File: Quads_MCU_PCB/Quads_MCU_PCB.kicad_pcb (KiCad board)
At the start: 4 copper layers, 100 x 100 mm, 108 parts, among them J1 USB_C_Receptacle_USB2.0_16P, J2 Conn_01x06_Pin, J3 Conn_01x02_Pin, J4 Conn_01x04_Pin, J5 Conn_01x04_Pin, J6 Conn_01x04_Pin, J7 Conn_01x04_Pin, SW1 SW_Push, U1 STM32H723ZGTx, U10 BMI088, U3 ADM3057ExRW, U4 TSR_1-2450, U5 AP7361C-33E, U6 ADM3057ExRW, U7 ADM3057ExRW, U8 MCP2518FD-xQBB, U9 ADM3057ExRW, Y1 40MHz, Y2 25MHz

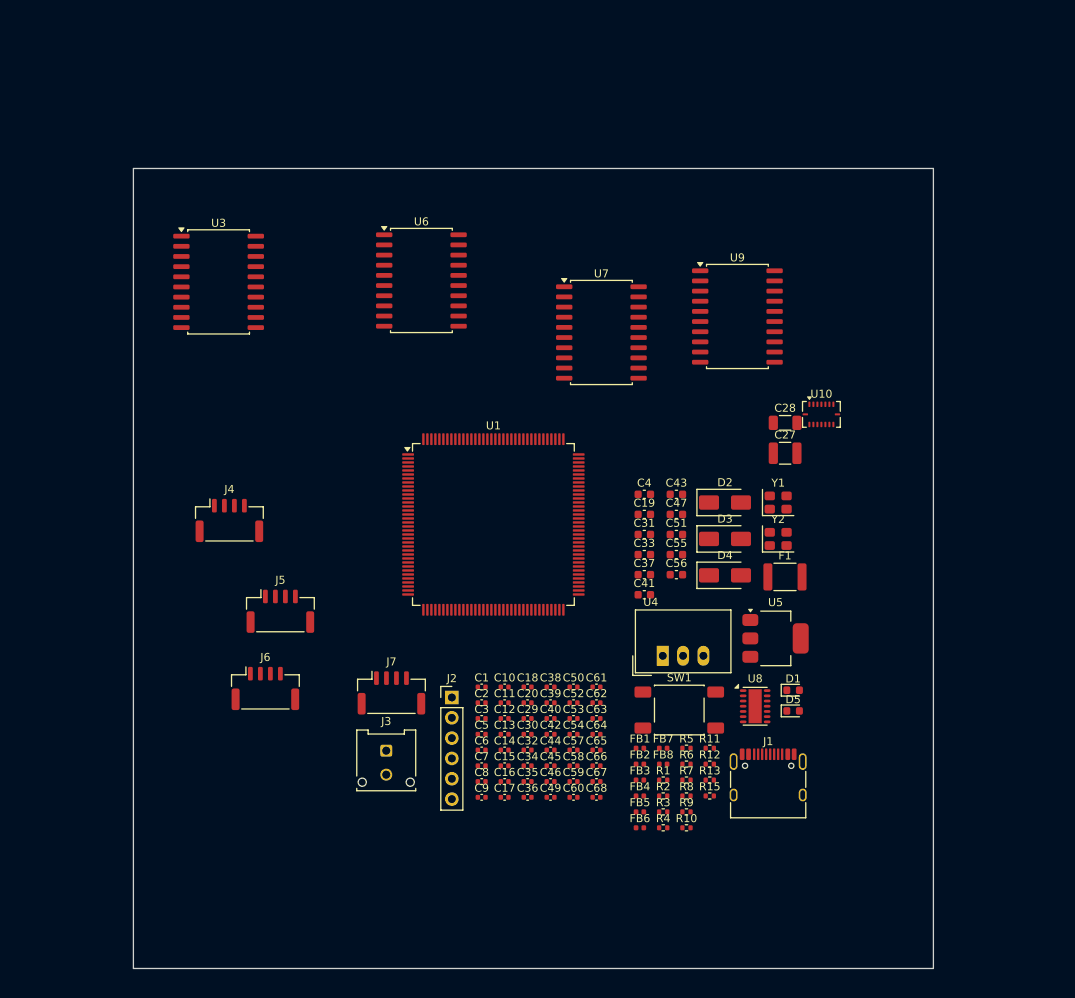
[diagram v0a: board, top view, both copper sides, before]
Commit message: Updated pwr connector footprint & added 3d model
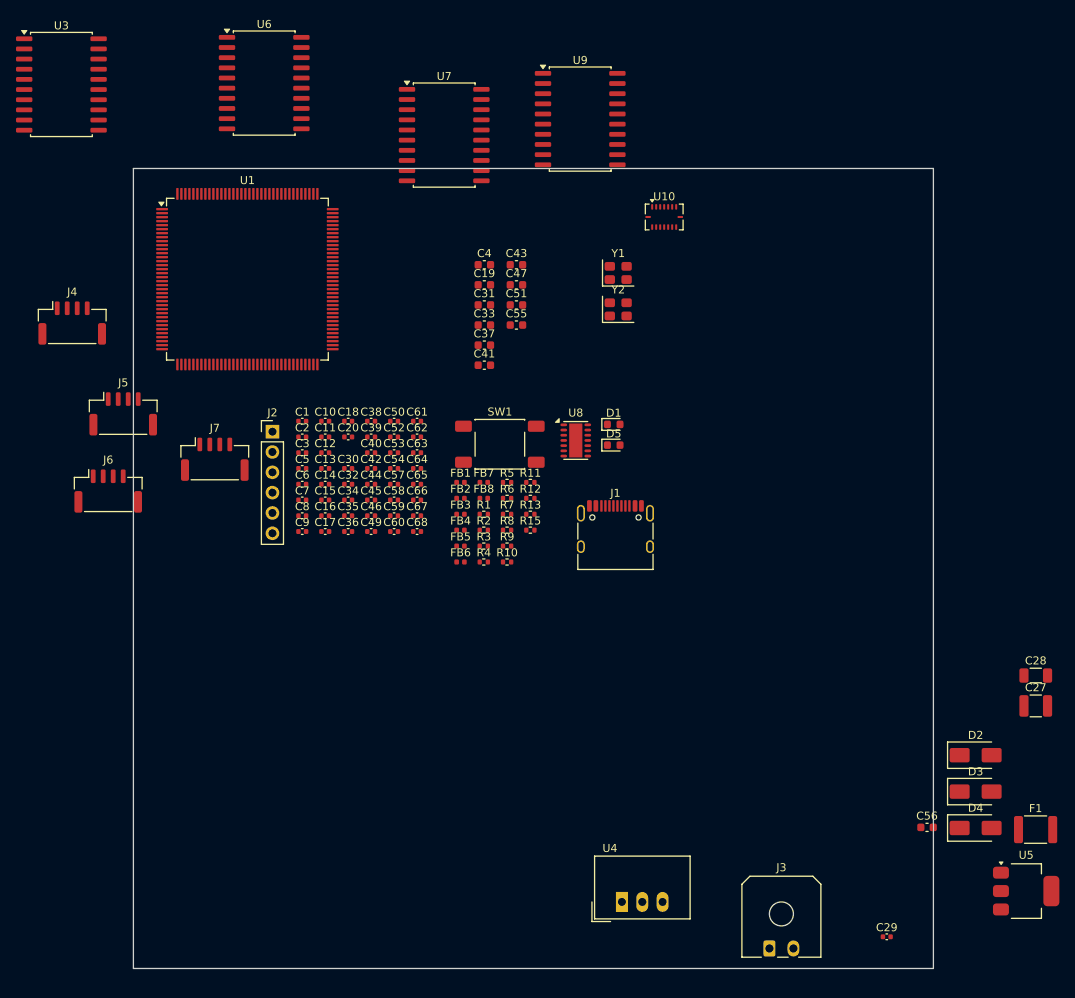
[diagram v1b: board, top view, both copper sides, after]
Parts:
- J3: footprint Connector_Molex:Molex_Micro-Fit_3.0_43045-0212_2x01_P3.00mm_Vertical -> Connector_Molex:Molex_Micro-Fit_3.0_43650-0200_1x02_P3.00mm_Horizontal
- moved J3 53.9 mm to (113.5, 136.0)
- moved C29 52.5 mm to (128.2, 134.5)
- moved C56 44.5 mm to (133.2, 120.9)
- moved F1 44.5 mm to (146.8, 121.1)
- moved D2 44.5 mm to (139.3, 111.8)
- moved D3 44.5 mm to (139.3, 116.4)
- moved D4 44.5 mm to (139.3, 120.9)
- moved U5 44.5 mm to (145.6, 128.8)
- moved C27 44.5 mm to (146.8, 105.7)
- moved C28 44.5 mm to (146.8, 101.9)
- moved U1 43.4 mm to (48.2, 52.3)
- moved C66 40.1 mm to (69.5, 79.9)
- moved C67 40.1 mm to (69.5, 81.9)
- moved C68 40.1 mm to (69.5, 83.9)
- moved R10 40.1 mm to (80.7, 87.7)
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
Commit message: Updated molex connector position
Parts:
- moved J3 8.06 mm to (117.5, 129.0), turned to 180 degrees
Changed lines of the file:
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@@
 	(footprint "Connector_Molex:Molex_Micro-Fit_3.0_43650-0200_1x02_P3.00mm_Horizontal"
 		(layer "F.Cu")
-		(at 113.5 136)
+		(at 117.5 129 180)
 		(descr "Molex Micro-Fit 3.0 Connector System, 43650-0200 (compatible alternatives: 43650-0201, 43650-0202), 2 Pins per row (https://www.molex.com/pdm_docs/sd/436500300_sd.pdf)")
 		(tags "connector Molex Micro-Fit_3.0 horizontal")
@@
 		)
 		(property "LCSC" "C293362"
-			(at 0 0 0)
+			(at 0 0 180)
 			(unlocked yes)
 			(layer "F.Fab")
@@
 		(duplicate_pad_numbers_are_jumpers no)
 		(fp_line
+			(start 6.435 1.09)
+			(end 3.651767 1.09)
+			(stroke
+				(width 0.12)
+				(type solid)
+			)
+			(layer "F.SilkS")
+		)
+		(fp_line
+			(start 6.435 -8.03)
+			(end 6.435 1.09)
+			(stroke
+				(width 0.12)
+				(type solid)
+			)
+			(layer "F.SilkS")
+		)
+		(fp_line
+			(start 5.435 -9.03)
+			(end 6.435 -8.03)
+			(stroke
+				(width 0.12)
+				(type solid)
+			)
+			(layer "F.SilkS")
+		)
+		(fp_line
+			(start 1.01 1.09)
+			(end 2.348233 1.09)
+			(stroke
+				(width 0.12)
+				(type solid)
+			)
+			(layer "F.SilkS")
+		)
+		(fp_line
+			(start -2.435 -9.03)
+			(end 5.435 -9.03)
+			(stroke
+				(width 0.12)
+				(type solid)
+			)
+			(layer "F.SilkS")
+		)
+		(fp_line
+			(start -3.435 1.09)
+			(end -1.01 1.09)
+			(stroke
+				(width 0.12)
+				(type solid)
+			)
+			(layer "F.SilkS")
+		)
+		(fp_line
+			(start -3.435 1.09)
+			(end -3.435 -8.03)
+			(stroke
+				(width 0.12)
+				(type solid)
+			)
+			(layer "F.SilkS")
+		)
+		(fp_line
 			(start -3.435 -8.03)
 			(end -2.435 -9.03)
@@
 		)
 		(fp_line
-			(start -3.435 1.09)
-			(end -3.435 -8.03)
-			(stroke
-				(width 0.12)
-				(type solid)
-			)
-			(layer "F.SilkS")
-		)
-		(fp_line
-			(start -3.435 1.09)
-			(end -1.01 1.09)
-			(stroke
-				(width 0.12)
-				(type solid)
-			)
-			(layer "F.SilkS")
-		)
-		(fp_line
-			(start -2.435 -9.03)
-			(end 5.435 -9.03)
-			(stroke
-				(width 0.12)
-				(type solid)
-			)
-			(layer "F.SilkS")
-		)
-		(fp_line
-			(start 1.01 1.09)
-			(end 2.348233 1.09)
-			(stroke
-				(width 0.12)
-				(type solid)
-			)
-			(layer "F.SilkS")
-		)
-		(fp_line
-			(start 5.435 -9.03)
-			(end 6.435 -8.03)
-			(stroke
-				(width 0.12)
-				(type solid)
-			)
-			(layer "F.SilkS")
-		)
-		(fp_line
-			(start 6.435 -8.03)
-			(end 6.435 1.09)
-			(stroke
-				(width 0.12)
-				(type solid)
-			)
-			(layer "F.SilkS")
-		)
-		(fp_line
-			(start 6.435 1.09)
-			(end 3.651767 1.09)
-			(stroke
-				(width 0.12)
-				(type solid)
-			)
-			(layer "F.SilkS")
+			(start 6.83 1.49)
+			(end -3.83 1.49)
+			(stroke
+				(width 0.05)
+				(type solid)
+			)
+			(layer "F.CrtYd")
+		)
+		(fp_line
+			(start 6.83 -9.42)
+			(end 6.83 1.49)
+			(stroke
+				(width 0.05)
+				(type solid)
+			)
+			(layer "F.CrtYd")
+		)
+		(fp_line
+			(start -3.83 1.49)
+			(end -3.83 -9.42)
+			(stroke
+				(width 0.05)
+				(type solid)
+			)
+			(layer "F.CrtYd")
 		)
 		(fp_line
@@
 		)
 		(fp_line
-			(start -3.83 1.49)
-			(end -3.83 -9.42)
-			(stroke
-				(width 0.05)
-				(type solid)
-			)
-			(layer "F.CrtYd")
-		)
-		(fp_line
-			(start 6.83 -9.42)
-			(end 6.83 1.49)
-			(stroke
-				(width 0.05)
-				(type solid)
-			)
-			(layer "F.CrtYd")
-		)
-		(fp_line
-			(start 6.83 1.49)
-			(end -3.83 1.49)
-			(stroke
-				(width 0.05)
-				(type solid)
-			)
-			(layer "F.CrtYd")
+			(start 6.325 0.98)
+			(end -3.325 0.98)
+			(stroke
+				(width 0.1)
+				(type solid)
+			)
+			(layer "F.Fab")
+		)
+		(fp_line
+			(start 6.325 -7.92)
+			(end 6.325 0.98)
+			(stroke
+				(width 0.1)
+				(type solid)
+			)
+			(layer "F.Fab")
+		)
+		(fp_line
+			(start 5.325 -8.92)
+			(end 6.325 -7.92)
+			(stroke
+				(width 0.1)
+				(type solid)
+			)
+			(layer "F.Fab")
+		)
+		(fp_line
+			(start 0 0)
+			(end 0.75 0.98)
+			(stroke
+				(width 0.1)
+				(type solid)
+			)
+			(layer "F.Fab")
+		)
+		(fp_line
+			(start -0.75 0.98)
+			(end 0 0)
+			(stroke
+				(width 0.1)
+				(type solid)
+			)
+			(layer "F.Fab")
+		)
+		(fp_line
+			(start -2.325 -8.92)
+			(end 5.325 -8.92)
+			(stroke
+				(width 0.1)
+				(type solid)
+			)
+			(layer "F.Fab")
+		)
+		(fp_line
+			(start -3.325 0.98)
+			(end -3.325 -7.92)
+			(stroke
+				(width 0.1)
+				(type solid)
+			)
+			(layer "F.Fab")
 		)
 		(fp_line
@@
 			(layer "F.Fab")
 		)
-		(fp_line
-			(start -3.325 0.98)
-			(end -3.325 -7.92)
-			(stroke
-				(width 0.1)
-				(type solid)
-			)
-			(layer "F.Fab")
-		)
-		(fp_line
-			(start -2.325 -8.92)
-			(end 5.325 -8.92)
-			(stroke
-				(width 0.1)
-				(type solid)
-			)
-			(layer "F.Fab")
-		)
-		(fp_line
-			(start -0.75 0.98)
-			(end 0 0)
-			(stroke
-				(width 0.1)
-				(type solid)
-			)
-			(layer "F.Fab")
-		)
-		(fp_line
-			(start 0 0)
-			(end 0.75 0.98)
-			(stroke
-				(width 0.1)
-				(type solid)
-			)
-			(layer "F.Fab")
-		)
-		(fp_line
-			(start 5.325 -8.92)
-			(end 6.325 -7.92)
-			(stroke
-				(width 0.1)
-				(type solid)
-			)
-			(layer "F.Fab")
-		)
-		(fp_line
-			(start 6.325 -7.92)
-			(end 6.325 0.98)
-			(stroke
-				(width 0.1)
-				(type solid)
-			)
-			(layer "F.Fab")
-		)
-		(fp_line
-			(start 6.325 0.98)
-			(end -3.325 0.98)
-			(stroke
-				(width 0.1)
-				(type solid)
-			)
-			(layer "F.Fab")
-		)
 		(fp_text user "${REFERENCE}"
 			(at 1.5 -8.22 0)
@@
 		)
 		(pad "" np_thru_hole circle
-			(at 1.5 -4.32)
+			(at 1.5 -4.32 180)
 			(size 3 3)
 			(drill 3)
@@
 		)
 		(pad "1" thru_hole roundrect
-			(at 0 0)
+			(at 0 0 180)
 			(size 1.5 2.02)
 			(drill 1.02)
@@
 		)
 		(pad "2" thru_hole oval
-			(at 3 0)
+			(at 3 0 180)
 			(size 1.5 2.02)
 			(drill 1.02)

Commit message: Cleaned up layout a bit
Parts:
- moved U3 94.0 mm to (116.7, 48.7)
- moved U6 67.4 mm to (105.7, 66.4)
- moved U7 59.3 mm to (122.2, 67.4)
- moved J5 36.3 mm to (49.5, 101.3)
- moved J4 36.3 mm to (43.2, 90.0)
- moved J6 36.3 mm to (47.7, 111.0)
- moved C56 28.3 mm to (110.3, 104.3)
- moved D2 28.3 mm to (116.3, 95.3)
- moved D3 28.3 mm to (116.3, 99.9)
- moved F1 28.3 mm to (123.8, 104.6)
- moved D4 28.3 mm to (116.3, 104.4)
- moved C29 28.3 mm to (105.2, 118.0)
- moved U5 28.3 mm to (122.7, 112.3)
- moved C27 18.0 mm to (130.5, 98.0)
- moved C28 18.0 mm to (130.5, 94.2)
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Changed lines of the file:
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@@
 	(footprint "Capacitor_SMD:C_0603_1608Metric"
 		(layer "F.Cu")
-		(at 77.87 53.05)
+		(at 66.775 45.98)
 		(descr "Capacitor SMD 0603 (1608 Metric), square (rectangular) end terminal, IPC-7351 nominal, (Body size source: IPC-SM-782 page 76, https://www.pcb-3d.com/wordpress/wp-content/uploads/ipc-sm-782a_amendment_1_and_2.pdf)")
 		(tags "capacitor")
@@
 	(footprint "Capacitor_SMD:C_0603_1608Metric"
 		(layer "F.Cu")
-		(at 77.87 50.54)
+		(at 66.775 43.47)
 		(descr "Capacitor SMD 0603 (1608 Metric), square (rectangular) end terminal, IPC-7351 nominal, (Body size source: IPC-SM-782 page 76, https://www.pcb-3d.com/wordpress/wp-content/uploads/ipc-sm-782a_amendment_1_and_2.pdf)")
 		(tags "capacitor")
@@
 	(footprint "Capacitor_SMD:C_0603_1608Metric"
 		(layer "F.Cu")
-		(at 77.87 55.56)
+		(at 66.775 48.49)
 		(descr "Capacitor SMD 0603 (1608 Metric), square (rectangular) end terminal, IPC-7351 nominal, (Body size source: IPC-SM-782 page 76, https://www.pcb-3d.com/wordpress/wp-content/uploads/ipc-sm-782a_amendment_1_and_2.pdf)")
 		(tags "capacitor")
@@
 	(footprint "Diode_SMD:D_SMA"
 		(layer "F.Cu")
-		(at 139.28 116.39)
+		(at 116.335 99.865)
 		(descr "Diode SMA (DO-214AC)")
 		(tags "Diode SMA (DO-214AC)")
@@
 	(footprint "Connector_JST:JST_GH_SM04B-GHS-TB_1x04-1MP_P1.25mm_Horizontal"
 		(layer "F.Cu")
-		(at 32.725 69.175)
+		(at 49.55 101.325)
 		(descr "JST GH series connector, SM04B-GHS-TB (http://www.jst-mfg.com/product/pdf/eng/eGH.pdf)")
 		(tags "connector JST GH horizontal")
@@
 	(footprint "Capacitor_SMD:C_1210_3225Metric"
 		(layer "F.Cu")
-		(at 146.795 105.68)
+		(at 130.525 98)
 		(descr "Capacitor SMD 1210 (3225 Metric), square (rectangular) end terminal, IPC-7351 nominal, (Body size source: IPC-SM-782 page 76, https://www.pcb-3d.com/wordpress/wp-content/uploads/ipc-sm-782a_amendment_1_and_2.pdf)")
 		(tags "capacitor")
@@
 	(footprint "Capacitor_SMD:C_1206_3216Metric"
 		(layer "F.Cu")
-		(at 146.795 101.88)
+		(at 130.525 94.2)
 		(descr "Capacitor SMD 1206 (3216 Metric), square (rectangular) end terminal, IPC-7351 nominal, (Body size source: IPC-SM-782 page 76, https://www.pcb-3d.com/wordpress/wp-content/uploads/ipc-sm-782a_amendment_1_and_2.pdf)")
 		(tags "capacitor")
@@
 	(footprint "Package_SO:SOIC-20W_7.5x12.8mm_P1.27mm"
 		(layer "F.Cu")
-		(at 25 28)
+		(at 116.65 48.675)
 		(descr "SOIC, 20 Pin (JEDEC MS-013AC, https://www.analog.com/media/en/package-pcb-resources/package/233848rw_20.pdf)")
 		(tags "SOIC SO")
@@
 	(footprint "Package_SO:SOIC-20W_7.5x12.8mm_P1.27mm"
 		(layer "F.Cu")
-		(at 50.35 27.825)
+		(at 105.65 66.365)
 		(descr "SOIC, 20 Pin (JEDEC MS-013AC, https://www.analog.com/media/en/package-pcb-resources/package/233848rw_20.pdf)")
 		(tags "SOIC SO")
@@
 	(footprint "Diode_SMD:D_SMA"
 		(layer "F.Cu")
-		(at 139.28 120.94)
+		(at 116.335 104.415)
 		(descr "Diode SMA (DO-214AC)")
 		(tags "Diode SMA (DO-214AC)")
@@
 	(footprint "Connector_JST:JST_GH_SM04B-GHS-TB_1x04-1MP_P1.25mm_Horizontal"
 		(layer "F.Cu")
-		(at 26.35 57.825)
+		(at 43.175 89.975)
 		(descr "JST GH series connector, SM04B-GHS-TB (http://www.jst-mfg.com/product/pdf/eng/eGH.pdf)")
 		(tags "connector JST GH horizontal")
@@
 	(footprint "Capacitor_SMD:C_0402_1005Metric"
 		(layer "F.Cu")
-		(at 128.17 134.54)
+		(at 105.225 118.015)
 		(descr "Capacitor SMD 0402 (1005 Metric), square (rectangular) end terminal, IPC-7351 nominal, (Body size source: IPC-SM-782 page 76, https://www.pcb-3d.com/wordpress/wp-content/uploads/ipc-sm-782a_amendment_1_and_2.pdf)")
 		(tags "capacitor")
@@
 		(tags "connector JST GH horizontal")
 		(property "Reference" "J7"
-			(at 0 -3.9 0)
+			(at 16.825 28.25 0)
 			(layer "F.SilkS")
 			(effects
@@
 		)
 		(fp_text user "${REFERENCE}"
-			(at 0 0 0)
+			(at 16.825 32.15 0)
 			(layer "F.Fab")
 			(effects
@@
 	(footprint "Package_TO_SOT_SMD:SOT-223-3_TabPin2"
 		(layer "F.Cu")
-		(at 145.595 128.825)
+		(at 122.65 112.3)
 		(descr "module CMS SOT223 4 pins")
 		(tags "CMS SOT")
@@
 	(footprint "Capacitor_SMD:C_0603_1608Metric"
 		(layer "F.Cu")
-		(at 77.87 58.07)
+		(at 66.775 51)
 		(descr "Capacitor SMD 0603 (1608 Metric), square (rectangular) end terminal, IPC-7351 nominal, (Body size source: IPC-SM-782 page 76, https://www.pcb-3d.com/wordpress/wp-content/uploads/ipc-sm-782a_amendment_1_and_2.pdf)")
 		(tags "capacitor")
@@
 	(footprint "Package_SO:SOIC-20W_7.5x12.8mm_P1.27mm"
 		(layer "F.Cu")
-		(at 89.85 32.325)
+		(at 85 49.5)
 		(descr "SOIC, 20 Pin (JEDEC MS-013AC, https://www.analog.com/media/en/package-pcb-resources/package/233848rw_20.pdf)")
 		(tags "SOIC SO")
@@
 		)
 		(fp_text user "${REFERENCE}"
-			(at 0 0 0)
+			(at 0 -0.5 0)
 			(layer "F.Fab")
 			(effects
@@
 	(footprint "Capacitor_SMD:C_0603_1608Metric"
 		(layer "F.Cu")
-		(at 77.87 60.58)
+		(at 66.775 53.51)
 		(descr "Capacitor SMD 0603 (1608 Metric), square (rectangular) end terminal, IPC-7351 nominal, (Body size source: IPC-SM-782 page 76, https://www.pcb-3d.com/wordpress/wp-content/uploads/ipc-sm-782a_amendment_1_and_2.pdf)")
 		(tags "capacitor")
@@
 	(footprint "Diode_SMD:D_SMA"
 		(layer "F.Cu")
-		(at 139.28 111.84)
+		(at 116.335 95.315)
 		(descr "Diode SMA (DO-214AC)")
 		(tags "Diode SMA (DO-214AC)")
@@
 	(footprint "Capacitor_SMD:C_0603_1608Metric"
 		(layer "F.Cu")
-		(at 81.88 55.56)
+		(at 70.785 48.49)
 		(descr "Capacitor SMD 0603 (1608 Metric), square (rectangular) end terminal, IPC-7351 nominal, (Body size source: IPC-SM-782 page 76, https://www.pcb-3d.com/wordpress/wp-content/uploads/ipc-sm-782a_amendment_1_and_2.pdf)")
 		(tags "capacitor")
@@
 	(footprint "Capacitor_SMD:C_0603_1608Metric"
 		(layer "F.Cu")
-		(at 77.87 63.09)
+		(at 66.775 56.02)
 		(descr "Capacitor SMD 0603 (1608 Metric), square (rectangular) end terminal, IPC-7351 nominal, (Body size source: IPC-SM-782 page 76, https://www.pcb-3d.com/wordpress/wp-content/uploads/ipc-sm-782a_amendment_1_and_2.pdf)")
 		(tags "capacitor")
@@
 	(footprint "Capacitor_SMD:C_0603_1608Metric"
 		(layer "F.Cu")
-		(at 133.205 120.86)
+		(at 110.26 104.335)
 		(descr "Capacitor SMD 0603 (1608 Metric), square (rectangular) end terminal, IPC-7351 nominal, (Body size source: IPC-SM-782 page 76, https://www.pcb-3d.com/wordpress/wp-content/uploads/ipc-sm-782a_amendment_1_and_2.pdf)")
 		(tags "capacitor")
@@
 	(footprint "Capacitor_SMD:C_0603_1608Metric"
 		(layer "F.Cu")
-		(at 81.88 53.05)
+		(at 70.785 45.98)
 		(descr "Capacitor SMD 0603 (1608 Metric), square (rectangular) end terminal, IPC-7351 nominal, (Body size source: IPC-SM-782 page 76, https://www.pcb-3d.com/wordpress/wp-content/uploads/ipc-sm-782a_amendment_1_and_2.pdf)")
 		(tags "capacitor")
@@
 	(footprint "Package_SO:SOIC-20W_7.5x12.8mm_P1.27mm"
 		(layer "F.Cu")
-		(at 72.85 34.325)
+		(at 122.15 67.365)
 		(descr "SOIC, 20 Pin (JEDEC MS-013AC, https://www.analog.com/media/en/package-pcb-resources/package/233848rw_20.pdf)")
 		(tags "SOIC SO")
@@
 	(footprint "Fuse:Fuse_1812_4532Metric"
 		(layer "F.Cu")
-		(at 146.775 121.14)
+		(at 123.83 104.615)
 		(descr "Fuse SMD 1812 (4532 Metric), square (rectangular) end terminal, IPC-7351 nominal, (Body size source: https://www.nikhef.nl/pub/departments/mt/projects/detectorR_D/dtddice/ERJ2G.pdf)")
 		(tags "fuse")
@@
 	(footprint "Capacitor_SMD:C_0603_1608Metric"
 		(layer "F.Cu")
-		(at 81.88 50.54)
+		(at 70.785 43.47)
 		(descr "Capacitor SMD 0603 (1608 Metric), square (rectangular) end terminal, IPC-7351 nominal, (Body size source: IPC-SM-782 page 76, https://www.pcb-3d.com/wordpress/wp-content/uploads/ipc-sm-782a_amendment_1_and_2.pdf)")
 		(tags "capacitor")
@@
 	(footprint "Capacitor_SMD:C_0603_1608Metric"
 		(layer "F.Cu")
-		(at 81.88 58.07)
+		(at 70.785 51)
 		(descr "Capacitor SMD 0603 (1608 Metric), square (rectangular) end terminal, IPC-7351 nominal, (Body size source: IPC-SM-782 page 76, https://www.pcb-3d.com/wordpress/wp-content/uploads/ipc-sm-782a_amendment_1_and_2.pdf)")
 		(tags "capacitor")
@@
 	(footprint "Connector_JST:JST_GH_SM04B-GHS-TB_1x04-1MP_P1.25mm_Horizontal"
 		(layer "F.Cu")
-		(at 30.85 78.825)
+		(at 47.675 110.975)
 		(descr "JST GH series connector, SM04B-GHS-TB (http://www.jst-mfg.com/product/pdf/eng/eGH.pdf)")
 		(tags "connector JST GH horizontal")
